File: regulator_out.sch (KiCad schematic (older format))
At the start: 36 parts

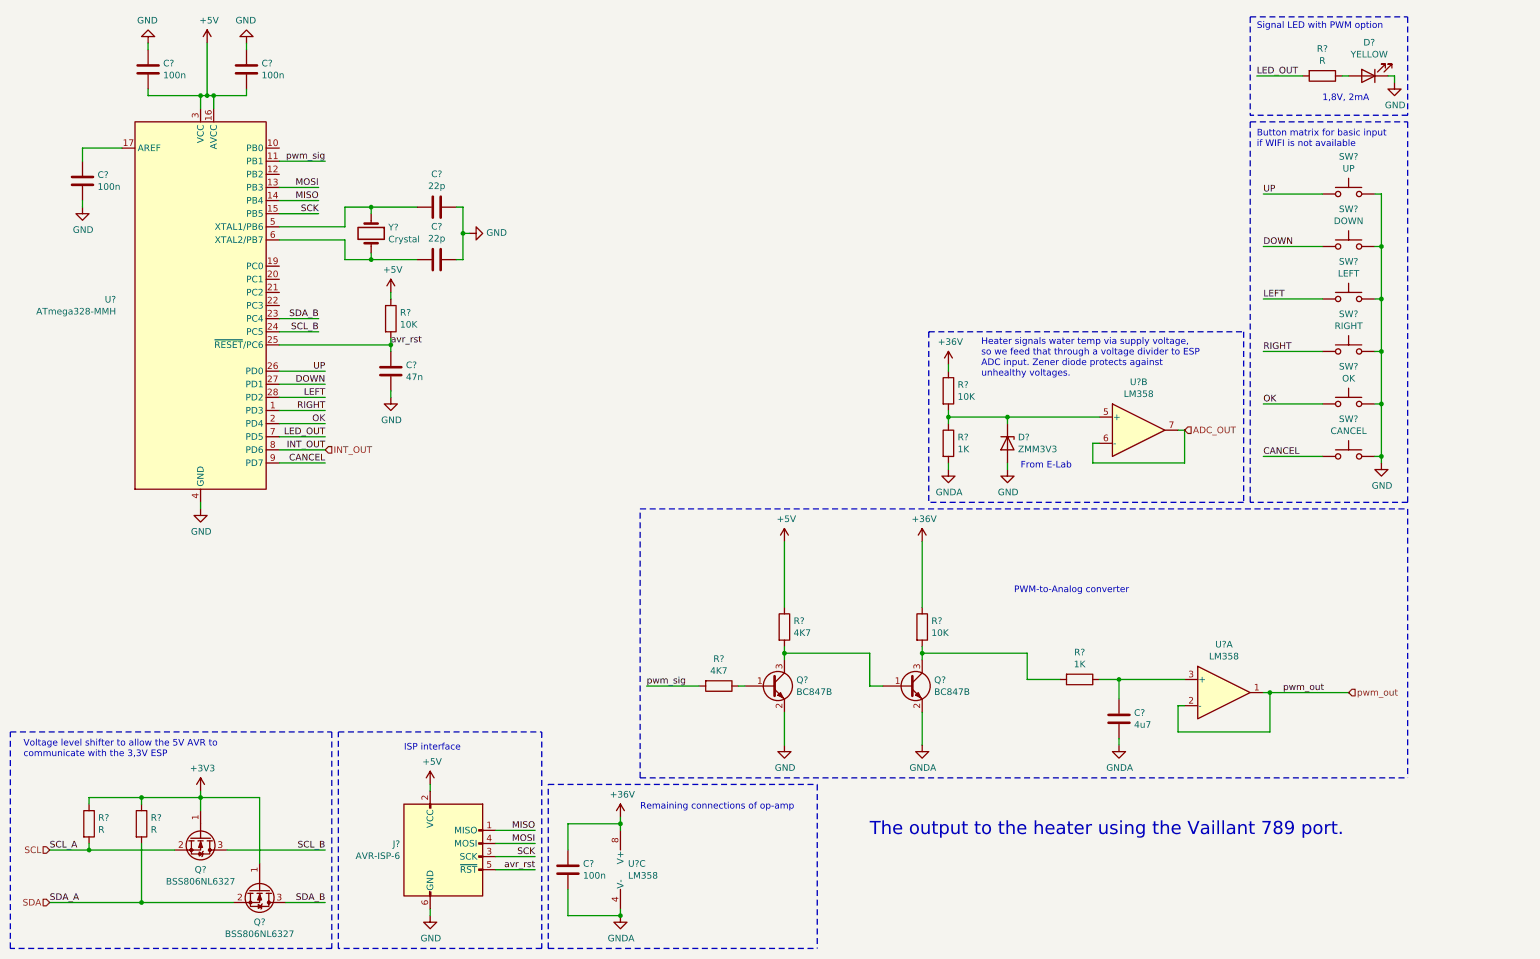
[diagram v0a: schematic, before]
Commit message: Added RTC for timekeeping, AVR can now measure supply voltage.
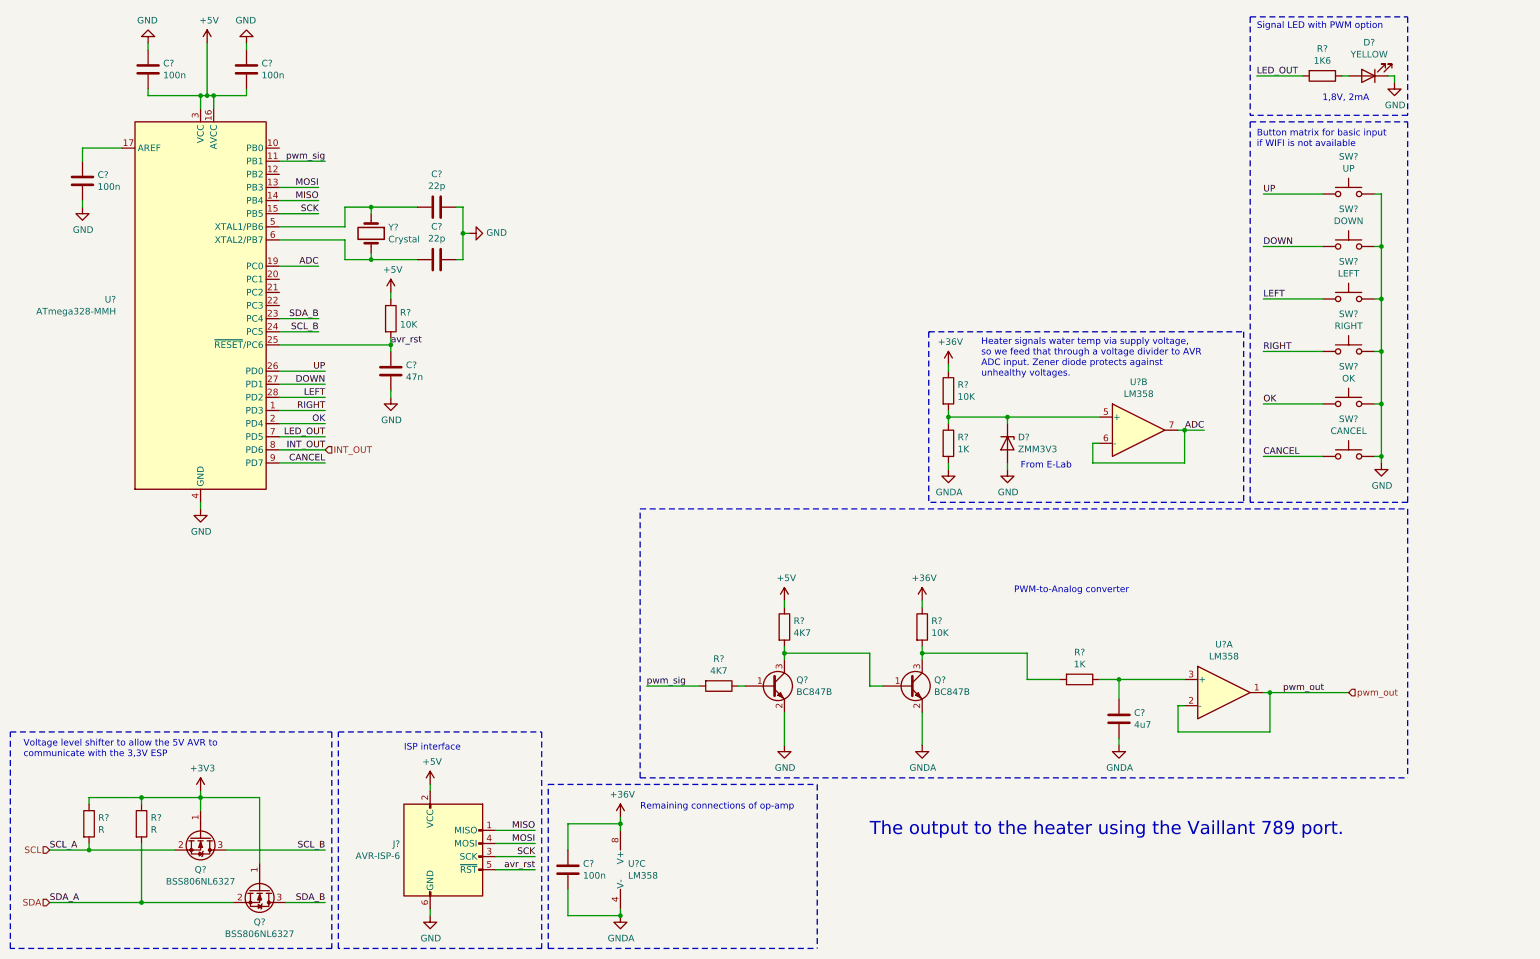
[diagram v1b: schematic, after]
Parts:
- R?: value R -> 1K6
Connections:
- net ADC_OUT is gone; now on net ADC: U?.6 (-), U?.7
- net ADC: now reaches U?.19 (PC0)
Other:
- note added: "Heater signals water temp via supply voltage, \nso we feed that through a voltage divider to AVR \nADC input. Zener diode protects against \nunhealthy voltages."
- note removed: "Heater signals water temp via supply voltage, \nso we feed that through a voltage divider to ESP \nADC input. Zener diode protects against \nunhealthy voltages."
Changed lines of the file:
@@
 	5350 5750 5750 5750
 Wire Wire Line
-	6400 4650 6400 5150
+	6400 5100 6400 5150
 $Comp
 L power:+5V #PWR?
 U 1 1 5E6D86F0
-P 6400 4650
-F 0 "#PWR?" H 6400 4500 50  0001 C CNN
-F 1 "+5V" H 6415 4823 50  0000 C CNN
-F 2 "" H 6400 4650 50  0001 C CNN
-F 3 "" H 6400 4650 50  0001 C CNN
-	1    6400 4650
+P 6400 5100
+F 0 "#PWR?" H 6400 4950 50  0001 C CNN
+F 1 "+5V" H 6415 5273 50  0000 C CNN
+F 2 "" H 6400 5100 50  0001 C CNN
+F 3 "" H 6400 5100 50  0001 C CNN
+	1    6400 5100
 	1    0    0    -1
 $EndComp
@@
 L power:+36V #PWR?
 U 1 1 5E7E489A
-P 7450 4650
-F 0 "#PWR?" H 7450 4500 50  0001 C CNN
-F 1 "+36V" H 7465 4823 50  0000 C CNN
-F 2 "" H 7450 4650 50  0001 C CNN
-F 3 "" H 7450 4650 50  0001 C CNN
-	1    7450 4650
-	1    0    0    -1
-$EndComp
-Wire Wire Line
-	7450 4650 7450 5150
+P 7450 5100
+F 0 "#PWR?" H 7450 4950 50  0001 C CNN
+F 1 "+36V" H 7465 5273 50  0000 C CNN
+F 2 "" H 7450 5100 50  0001 C CNN
+F 3 "" H 7450 5100 50  0001 C CNN
+	1    7450 5100
+	1    0    0    -1
+$EndComp
+Wire Wire Line
+	7450 5100 7450 5150
 Wire Notes Line
 	5300 6450 5300 4400
@@
 P 10500 1100
 F 0 "R?" V 10293 1100 50  0000 C CNN
-F 1 "R" V 10384 1100 50  0000 C CNN
+F 1 "1K6" V 10384 1100 50  0000 C CNN
 F 2 "" V 10430 1100 50  0001 C CNN
 F 3 "~" H 10500 1100 50  0001 C CNN
@@
 U 1 1 5E8EF643
 P 8100 3900
+AR Path="/5E8EF643" Ref="D?"  Part="1"
+AR Path="/5E6A63AE/5E8EF643" Ref="D?"  Part="1"
 F 0 "D?" V 8054 3980 50  0000 L CNN
 F 1 "ZMM3V3" V 8145 3980 50  0000 L CNN
@@
 U 1 1 5E8EF649
 P 7650 3900
+AR Path="/5E8EF649" Ref="R?"  Part="1"
+AR Path="/5E6A63AE/5E8EF649" Ref="R?"  Part="1"
 F 0 "R?" H 7720 3946 50  0000 L CNN
 F 1 "1K" H 7720 3855 50  0000 L CNN
@@
 U 1 1 5E8EF64F
 P 7650 3500
+AR Path="/5E8EF64F" Ref="R?"  Part="1"
+AR Path="/5E6A63AE/5E8EF64F" Ref="R?"  Part="1"
 F 0 "R?" H 7720 3546 50  0000 L CNN
 F 1 "10K" H 7720 3455 50  0000 L CNN
@@
 U 1 1 5E8EF655
 P 7650 4100
+AR Path="/5E8EF655" Ref="#PWR?"  Part="1"
+AR Path="/5E6A63AE/5E8EF655" Ref="#PWR?"  Part="1"
 F 0 "#PWR?" H 7650 3850 50  0001 C CNN
 F 1 "GNDA" H 7655 3927 50  0000 C CNN
@@
 U 1 1 5E8EF65B
 P 8100 4100
+AR Path="/5E8EF65B" Ref="#PWR?"  Part="1"
+AR Path="/5E6A63AE/5E8EF65B" Ref="#PWR?"  Part="1"
 F 0 "#PWR?" H 8100 3850 50  0001 C CNN
 F 1 "GND" H 8105 3927 50  0000 C CNN
@@
 U 1 1 5E8EF661
 P 7650 3300
+AR Path="/5E8EF661" Ref="#PWR?"  Part="1"
+AR Path="/5E6A63AE/5E8EF661" Ref="#PWR?"  Part="1"
 F 0 "#PWR?" H 7650 3150 50  0001 C CNN
 F 1 "+36V" H 7665 3473 50  0000 C CNN
@@
 From E-Lab
 Text Notes 7900 3400 0    50   ~ 0
-Heater signals water temp via supply voltage, \nso we feed that through a voltage divider to ESP \nADC input. Zener diode protects against \nunhealthy voltages.
+Heater signals water temp via supply voltage, \nso we feed that through a voltage divider to AVR \nADC input. Zener diode protects against \nunhealthy voltages.
 Wire Wire Line
 	8100 3700 8800 3700
@@
 Wire Wire Line
 	9450 3800 9400 3800
-Text HLabel 9450 3800 2    50   Input ~ 0
-ADC_OUT
 Wire Notes Line
 	7500 3050 9900 3050
@@
 Text Notes 10500 1300 0    50   ~ 0
 1,8V, 2mA
+Text Label 9600 3800 2    50   ~ 0
+ADC
+Wire Wire Line
+	9600 3800 9450 3800
+Connection ~ 9450 3800
+Text Label 2850 2550 2    50   ~ 0
+ADC
+Wire Wire Line
+	2850 2550 2550 2550
 $EndSCHEMATC

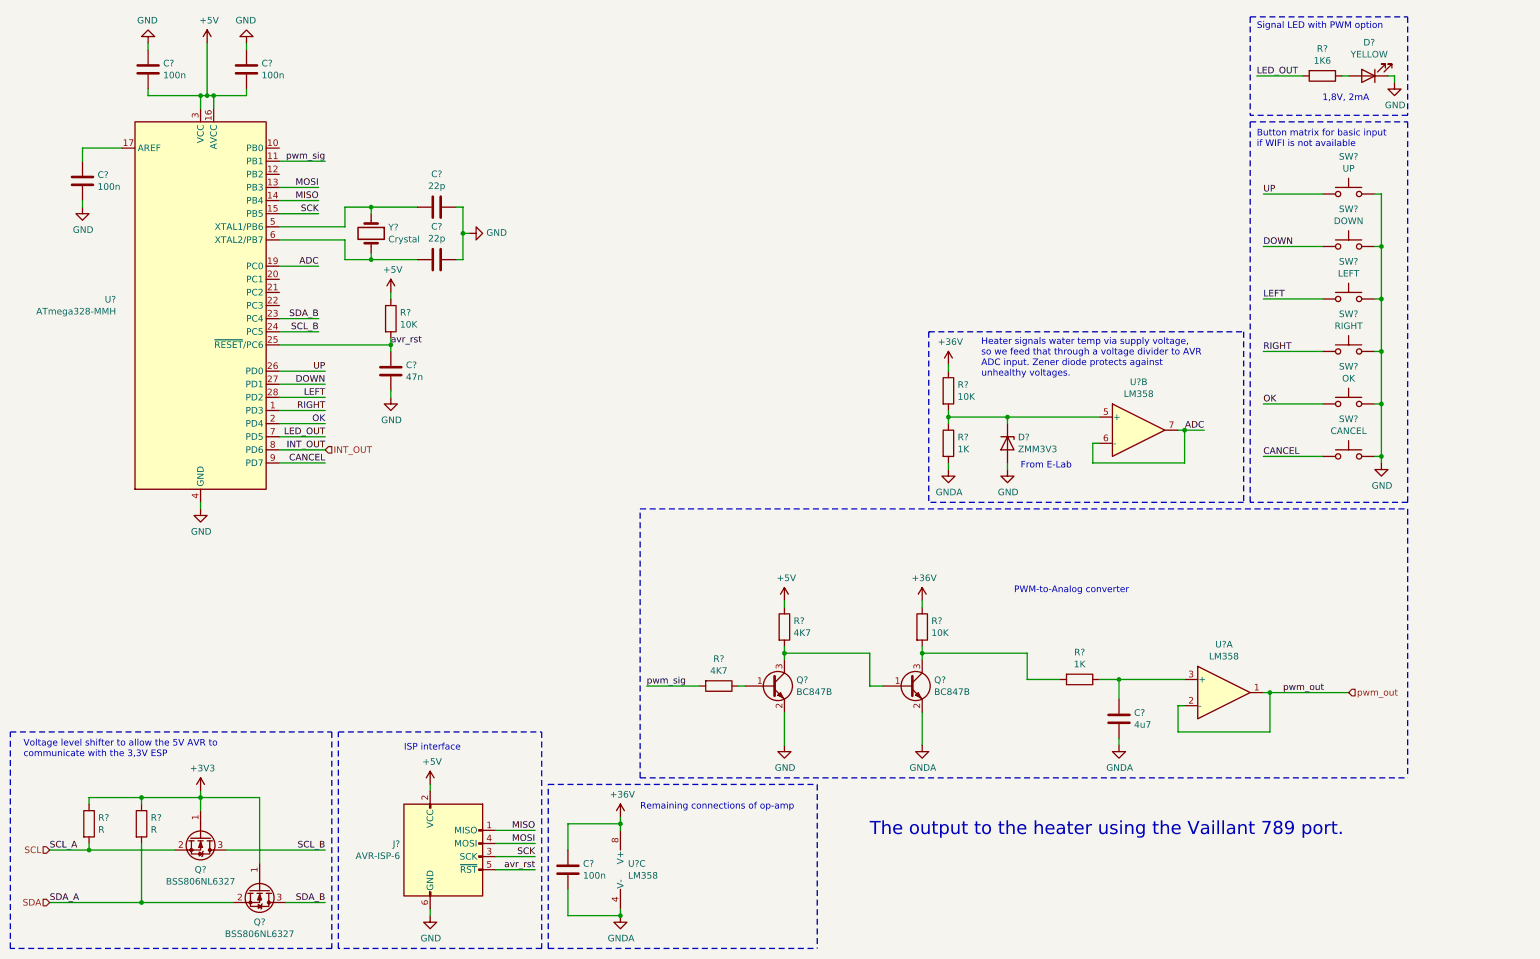
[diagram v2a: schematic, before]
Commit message: Added Temperature sensor.
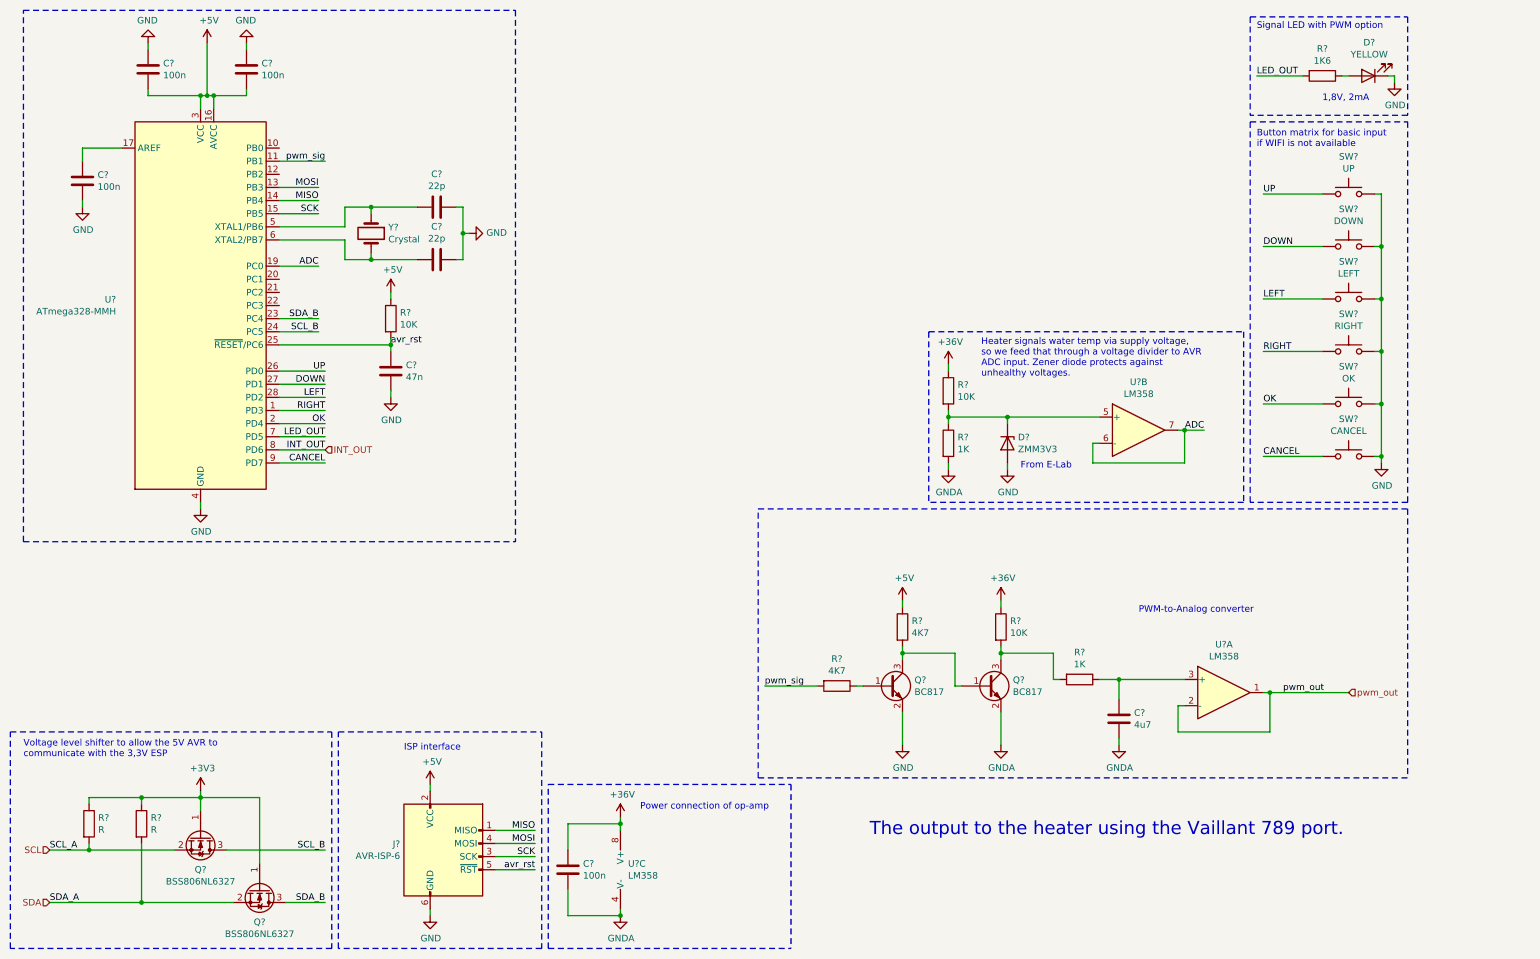
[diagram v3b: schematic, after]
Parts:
- Q? (x2): value BC847B -> BC817
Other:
- note added: "Power connection of op-amp"
- note removed: "Remaining connections of op-amp"
- moved on the sheet: Q?, R?
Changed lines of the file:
@@
 $Descr A4 11693 8268
 encoding utf-8
-Sheet 4 4
+Sheet 3 4
 Title ""
 Date ""
@@
 	1    0    0    -1
 $EndComp
-Text Label 5350 5750 0    50   ~ 0
+Text Label 6250 5750 0    50   ~ 0
 pwm_sig
 Wire Wire Line
-	5350 5750 5750 5750
-Wire Wire Line
-	6400 5100 6400 5150
+	6250 5750 6650 5750
+Wire Wire Line
+	7300 5100 7300 5150
 $Comp
 L power:+5V #PWR?
 U 1 1 5E6D86F0
-P 6400 5100
-F 0 "#PWR?" H 6400 4950 50  0001 C CNN
-F 1 "+5V" H 6415 5273 50  0000 C CNN
-F 2 "" H 6400 5100 50  0001 C CNN
-F 3 "" H 6400 5100 50  0001 C CNN
-	1    6400 5100
-	1    0    0    -1
-$EndComp
-Wire Wire Line
-	6050 5750 6100 5750
+P 7300 5100
+F 0 "#PWR?" H 7300 4950 50  0001 C CNN
+F 1 "+5V" H 7315 5273 50  0000 C CNN
+F 2 "" H 7300 5100 50  0001 C CNN
+F 3 "" H 7300 5100 50  0001 C CNN
+	1    7300 5100
+	1    0    0    -1
+$EndComp
+Wire Wire Line
+	6950 5750 7000 5750
 $Comp
 L power:GND #PWR?
 U 1 1 5E6D3024
-P 6400 6200
-F 0 "#PWR?" H 6400 5950 50  0001 C CNN
-F 1 "GND" H 6405 6027 50  0000 C CNN
-F 2 "" H 6400 6200 50  0001 C CNN
-F 3 "" H 6400 6200 50  0001 C CNN
-	1    6400 6200
+P 7300 6200
+F 0 "#PWR?" H 7300 5950 50  0001 C CNN
+F 1 "GND" H 7305 6027 50  0000 C CNN
+F 2 "" H 7300 6200 50  0001 C CNN
+F 3 "" H 7300 6200 50  0001 C CNN
+	1    7300 6200
 	1    0    0    -1
 $EndComp
@@
 L Device:R R?
 U 1 1 5E6AEB7F
-P 6400 5300
-F 0 "R?" H 6470 5346 50  0000 L CNN
-F 1 "4K7" H 6470 5255 50  0000 L CNN
-F 2 "" V 6330 5300 50  0001 C CNN
-F 3 "~" H 6400 5300 50  0001 C CNN
-	1    6400 5300
+P 7300 5300
+F 0 "R?" H 7370 5346 50  0000 L CNN
+F 1 "4K7" H 7370 5255 50  0000 L CNN
+F 2 "" V 7230 5300 50  0001 C CNN
+F 3 "~" H 7300 5300 50  0001 C CNN
+	1    7300 5300
 	1    0    0    -1
 $EndComp
@@
 L Device:R R?
 U 1 1 5E6AA7AC
-P 5900 5750
-F 0 "R?" V 5693 5750 50  0000 C CNN
-F 1 "4K7" V 5784 5750 50  0000 C CNN
-F 2 "" V 5830 5750 50  0001 C CNN
-F 3 "~" H 5900 5750 50  0001 C CNN
-	1    5900 5750
+P 6800 5750
+F 0 "R?" V 6593 5750 50  0000 C CNN
+F 1 "4K7" V 6684 5750 50  0000 C CNN
+F 2 "" V 6730 5750 50  0001 C CNN
+F 3 "~" H 6800 5750 50  0001 C CNN
+	1    6800 5750
 	0    1    1    0
 $EndComp
 Wire Wire Line
-	6400 5950 6400 6200
+	7300 5950 7300 6200
 $Comp
 L Device:R R?
 U 1 1 5E6CB37D
-P 7450 5300
-F 0 "R?" H 7520 5346 50  0000 L CNN
-F 1 "10K" H 7520 5255 50  0000 L CNN
-F 2 "" V 7380 5300 50  0001 C CNN
-F 3 "~" H 7450 5300 50  0001 C CNN
-	1    7450 5300
-	1    0    0    -1
-$EndComp
-Text Notes 8150 5050 0    50   ~ 0
+P 8050 5300
+F 0 "R?" H 8120 5346 50  0000 L CNN
+F 1 "10K" H 8120 5255 50  0000 L CNN
+F 2 "" V 7980 5300 50  0001 C CNN
+F 3 "~" H 8050 5300 50  0001 C CNN
+	1    8050 5300
+	1    0    0    -1
+$EndComp
+Text Notes 9100 5200 0    50   ~ 0
 PWM-to-Analog converter
 Wire Wire Line
-	6400 5450 6400 5500
-Wire Wire Line
-	6400 5500 7050 5500
-Wire Wire Line
-	7050 5500 7050 5750
-Wire Wire Line
-	7050 5750 7150 5750
-Connection ~ 6400 5500
-Wire Wire Line
-	6400 5500 6400 5550
+	7300 5450 7300 5500
+Wire Wire Line
+	7300 5500 7700 5500
+Wire Wire Line
+	7700 5500 7700 5750
+Wire Wire Line
+	7700 5750 7750 5750
+Connection ~ 7300 5500
+Wire Wire Line
+	7300 5500 7300 5550
 $Comp
 L power:GNDA #PWR?
 U 1 1 5E7DE66A
-P 7450 6200
-F 0 "#PWR?" H 7450 5950 50  0001 C CNN
-F 1 "GNDA" H 7455 6027 50  0000 C CNN
-F 2 "" H 7450 6200 50  0001 C CNN
-F 3 "" H 7450 6200 50  0001 C CNN
-	1    7450 6200
-	1    0    0    -1
-$EndComp
-Wire Wire Line
-	7450 6200 7450 5950
-Wire Wire Line
-	7450 5450 7450 5500
-Wire Wire Line
-	7450 5500 8250 5500
-Wire Wire Line
-	8250 5500 8250 5700
-Wire Wire Line
-	8250 5700 8500 5700
-Connection ~ 7450 5500
-Wire Wire Line
-	7450 5500 7450 5550
+P 8050 6200
+F 0 "#PWR?" H 8050 5950 50  0001 C CNN
+F 1 "GNDA" H 8055 6027 50  0000 C CNN
+F 2 "" H 8050 6200 50  0001 C CNN
+F 3 "" H 8050 6200 50  0001 C CNN
+	1    8050 6200
+	1    0    0    -1
+$EndComp
+Wire Wire Line
+	8050 6200 8050 5950
+Wire Wire Line
+	8050 5450 8050 5500
+Wire Wire Line
+	8050 5500 8450 5500
+Wire Wire Line
+	8450 5500 8450 5700
+Wire Wire Line
+	8450 5700 8500 5700
+Connection ~ 8050 5500
+Wire Wire Line
+	8050 5500 8050 5550
 $Comp
 L power:+36V #PWR?
 U 1 1 5E7E489A
-P 7450 5100
-F 0 "#PWR?" H 7450 4950 50  0001 C CNN
-F 1 "+36V" H 7465 5273 50  0000 C CNN
-F 2 "" H 7450 5100 50  0001 C CNN
-F 3 "" H 7450 5100 50  0001 C CNN
-	1    7450 5100
-	1    0    0    -1
-$EndComp
-Wire Wire Line
-	7450 5100 7450 5150
-Wire Notes Line
-	5300 6450 5300 4400
-Wire Notes Line
-	5300 4400 11150 4400
+P 8050 5100
+F 0 "#PWR?" H 8050 4950 50  0001 C CNN
+F 1 "+36V" H 8065 5273 50  0000 C CNN
+F 2 "" H 8050 5100 50  0001 C CNN
+F 3 "" H 8050 5100 50  0001 C CNN
+	1    8050 5100
+	1    0    0    -1
+$EndComp
+Wire Wire Line
+	8050 5100 8050 5150
+Wire Notes Line
+	6200 6450 6200 4400
+Wire Notes Line
+	6200 4400 11150 4400
 Wire Notes Line
 	11150 4400 11150 6450
 Wire Notes Line
-	5300 6450 11150 6450
+	6200 6450 11150 6450
 $Comp
 L power:+36V #PWR?
@@
 	5150 6800 5150 6850
 Text Notes 5300 6700 0    50   ~ 0
-Remaining connections of op-amp
+Power connection of op-amp
 Wire Notes Line
 	4600 7750 4600 6500
 Wire Notes Line
-	4600 6500 6650 6500
-Wire Notes Line
-	6650 6500 6650 7750
-Wire Notes Line
-	4600 7750 6650 7750
+	4600 6500 6450 6500
+Wire Notes Line
+	6450 6500 6450 7750
+Wire Notes Line
+	4600 7750 6450 7750
 $Comp
 L Device:Crystal Y?
@@
 L Device:Q_NPN_BEC Q?
 U 1 1 5E8E1AB8
-P 6300 5750
-F 0 "Q?" H 6491 5796 50  0000 L CNN
-F 1 "BC847B" H 6491 5705 50  0000 L CNN
-F 2 "" H 6500 5850 50  0001 C CNN
-F 3 "~" H 6300 5750 50  0001 C CNN
-	1    6300 5750
+P 7200 5750
+F 0 "Q?" H 7391 5796 50  0000 L CNN
+F 1 "BC817" H 7391 5705 50  0000 L CNN
+F 2 "" H 7400 5850 50  0001 C CNN
+F 3 "https://www.mouser.de/datasheet/2/916/BC817_SER-1598763.pdf" H 7200 5750 50  0001 C CNN
+	1    7200 5750
 	1    0    0    -1
 $EndComp
@@
 L Device:Q_NPN_BEC Q?
 U 1 1 5E8E2163
-P 7350 5750
-F 0 "Q?" H 7541 5796 50  0000 L CNN
-F 1 "BC847B" H 7541 5705 50  0000 L CNN
-F 2 "" H 7550 5850 50  0001 C CNN
-F 3 "~" H 7350 5750 50  0001 C CNN
-	1    7350 5750
+P 7950 5750
+F 0 "Q?" H 8141 5796 50  0000 L CNN
+F 1 "BC817" H 8141 5705 50  0000 L CNN
+F 2 "" H 8150 5850 50  0001 C CNN
+F 3 "https://www.mouser.de/datasheet/2/916/BC817_SER-1598763.pdf" H 7950 5750 50  0001 C CNN
+	1    7950 5750
 	1    0    0    -1
 $EndComp
@@
 Wire Wire Line
 	2850 2550 2550 2550
+Wire Notes Line
+	600  4650 600  600
+Wire Notes Line
+	600  600  4350 600
+Wire Notes Line
+	4350 600  4350 4650
+Wire Notes Line
+	600  4650 4350 4650
 $EndSCHEMATC
